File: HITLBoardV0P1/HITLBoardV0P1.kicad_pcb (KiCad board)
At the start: 2 copper layers, 269 parts, among them J2 FTSH-105-01-L-DV, Q1 NPN, Q2 PMOS, Q3 NPN, Q4 PMOS, SW1 SW_Push, SW2 SW_Push, U1 TMDX570LC43HDK_Connectors, U10 DAC7750IPWPR, U11 NC7SZ04P5X, U12 SN74LVC1G08DCKR, U13 NC7SZ04P5X, U14 SN74LVC1G08DCKR, U15 DAC7750IPWPR, U16 NC7SZ04P5X, U17 SN74LVC1G08DCKR, U18 DAC7750IPWPR, U19 NC7SZ04P5X, U2 LAN8650B1-E/LMX, U20 SN74LVC1G08DCKR, U21 DAC7750IPWPR, U22 TLV4387PWR, U23 ADS131M04QPWRQ1, U24 MCP23008-E/SO, U3 LP38852MRX-ADJ/NOPB, U4 LAN8650B1-E/LMX, U5 LP38852MRX-ADJ/NOPB, U6 LAN8650B1-E/LMX, U7 LP38852MRX-ADJ/NOPB, U8 LAN8650B1-E/LMX, U9 LP38852MRX-ADJ/NOPB

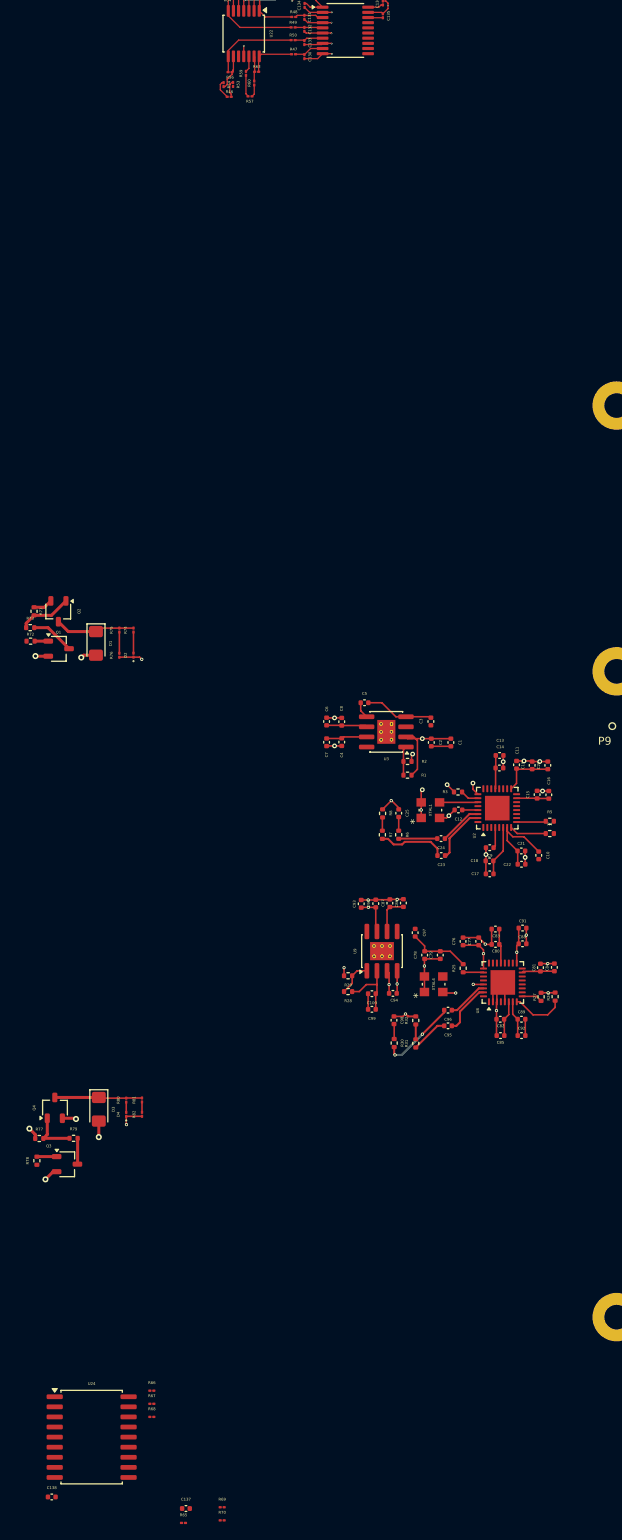
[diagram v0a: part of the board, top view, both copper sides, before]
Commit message: FIX spi 3 on tmdx for current loop ADC, add gpio pin for data ready
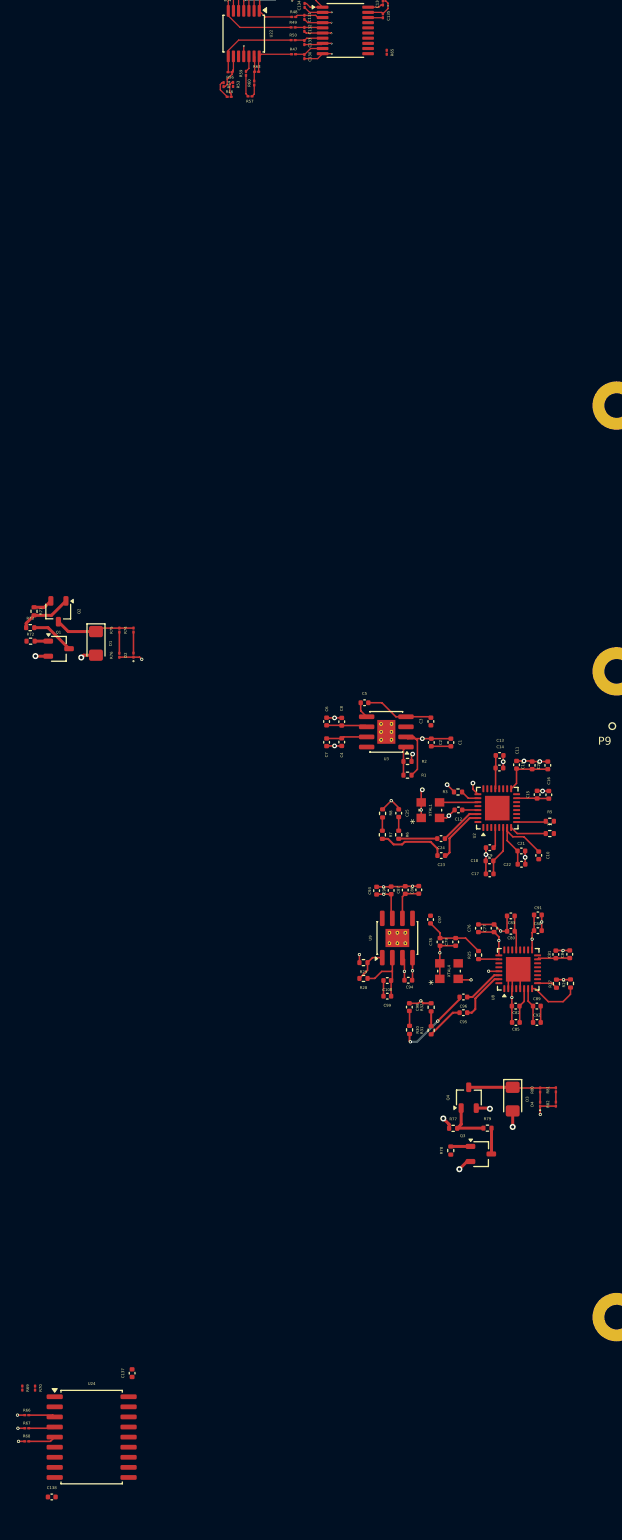
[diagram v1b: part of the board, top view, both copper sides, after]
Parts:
- moved R65 186.9 mm to (95.6, 45.4), turned to -90 degrees
- moved D3 52.1 mm to (111.5, 177.2)
- moved Q4 52.1 mm to (105.9, 177.0)
- moved D4 52.1 mm to (114.9, 177.9)
- moved Q3 52.1 mm to (107.5, 184.1)
- moved R77 52.1 mm to (104.0, 180.9)
- moved R78 52.1 mm to (103.7, 183.7)
- moved R79 52.1 mm to (108.3, 180.9)
- moved R80 52.1 mm to (114.9, 176.1)
- moved R81 52.1 mm to (116.9, 176.0)
- moved R82 52.1 mm to (116.9, 177.8)
- moved R69 29.3 mm to (49.7, 213.6), turned to -90 degrees
- moved R70 28.8 mm to (51.3, 213.6), turned to -90 degrees
- moved C137 18.3 mm to (63.6, 211.7), turned to 90 degrees
- moved R66 16.0 mm to (50.3, 217.0)
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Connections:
- net /TMDX_Breakout/SPI5_CS1_NR renamed /TMDX_Breakout/SPI5_CS1_N
- C137 pad 1: unconnected-(C137-Pad1) -> +3V3
- R68 pad 2: /I2C_GPIO_EXPANDER/<NO NET> -> /I2C_GPIO_EXPANDER/A0
- U1 pad P9-16: /TMDX_Breakout/SPI5_SCLK -> /TMDX_SPI5_SCLK
- U1 pad P9-18: /TMDX_Breakout/SPI5_CS0_N -> /TMDX_SPI5_CS0_N
- U1 pad P9-21: /TMDX_Breakout/SPI5_SIMO_0 -> /TMDX_SPI5_SIMO
- U1 pad P9-22: /TMDX_Breakout/SPI5_SOMI_0 -> /TMDX_SPI5_SOMI
- U24 pad 5: unconnected-(U24-A0-Pad5) -> /I2C_GPIO_EXPANDER/A0
- U8 pad 10: /TMDX_SPI1_SOMI -> /TMDX_SPI5_SOMI
- U8 pad 11: /TMDX_SPI1_CS1 -> /TMDX_SPI5_CS0_N
- U8 pad 12: /TMDX_SPI1_SCLK -> /TMDX_SPI5_SCLK
- U8 pad 13: /TMDX_SPI1_SIMO -> /TMDX_SPI5_SIMO
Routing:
- net /I2C_GPIO_EXPANDER/A1: track 0.00 -> 3.58 mm
- net /I2C_GPIO_EXPANDER/A0: track 0.00 -> 3.49 mm
- net /I2C_GPIO_EXPANDER/A2: track 0.00 -> 3.36 mm
- net GND: track 290.1 -> 292.7 mm, vias 92 -> 95

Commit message: basic organization into layout
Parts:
- removed R84: 10K, Resistor_SMD:R_01005_0402Metric
- removed SW2: SW_Push, Button_Switch_SMD:SW_Push_1P1T_NO_E-Switch_TL3301NxxxxxG
- moved R69 298.8 mm to (330.4, 111.0)
- moved C138 297.8 mm to (333.0, 124.5)
- moved R66 297.8 mm to (329.8, 114.2)
- moved R67 297.8 mm to (329.8, 115.8)
- moved R68 297.8 mm to (329.8, 117.5)
- moved U24 297.8 mm to (338.0, 116.9)
- moved R70 295.9 mm to (328.8, 111.0)
- moved R62 230.0 mm to (253.1, 183.3), turned to 180 degrees
- moved R58 229.9 mm to (252.2, 184.4), turned to 180 degrees
- moved R64 228.6 mm to (253.1, 182.2), turned to 0 degrees
- moved R45 227.2 mm to (249.8, 185.0), turned to 0 degrees
- moved R61 226.8 mm to (251.7, 182.5), turned to 90 degrees
- moved R51 226.3 mm to (250.5, 183.5), turned to 90 degrees
- moved R52 224.4 mm to (249.3, 183.5), turned to 90 degrees
- moved R55 222.5 mm to (249.3, 182.0), turned to 180 degrees
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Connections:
- net /ADC_DRDY renamed /CurrentInstrument/DATA_READY
- C136 pad 1: Net-(U23-DVDD) -> +3V3
- C69 pad 1: +5V -> /ethernet3/U3_BIAS
- R65 pad 1: /ADC_CS_N -> /TMDX_SPI3_CS1_N
- U1 pad P11-73: unconnected-(U1C-SPI3_SIMO-PadP11-73) -> /TMDX_SPI3_SIMO
- U1 pad P11-74: unconnected-(U1C-SPI3_SOMI-PadP11-74) -> /TMDX_SPI3_SOMI
- U1 pad P11-75: unconnected-(U1C-SPI3_CS1_NHET125-PadP11-75) -> /TMDX_SPI3_CS1_N
- U1 pad P11-78: unconnected-(U1C-SPI3_CLK-PadP11-78) -> /TMDX_SPI3_SCLK
- U23 pad 12: /ADC_CS_N -> /TMDX_SPI3_CS1_N
- U23 pad 14: /CurrentInstrument/SCLK -> /TMDX_SPI3_SCLK
- U23 pad 15: /CurrentInstrument/SDO -> /TMDX_SPI3_SOMI
- U23 pad 16: /CurrentInstrument/SDI -> /TMDX_SPI3_SIMO
- U23 pad 20: Net-(U23-DVDD) -> +3V3
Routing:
- net /RPI_I2C_SDA: track 0.00 -> 5.30 mm
- net /RPI_I2C_SCL: track 0.00 -> 3.20 mm
- net +3.3VP: track 30.7 -> 33.5 mm, vias 6 -> 9
- net +3V3: track 151.1 -> 153.8 mm, vias 26 -> 27
- net /TMDX_SPI3_CS1_N: track 0.00 -> 2.44 mm
- net Net-(U23-DVDD): track 1.98 -> 0.00 mm
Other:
- board outline added: 275.4 x 125.2 mm
- board text removed: "RPI BOOTSEL"

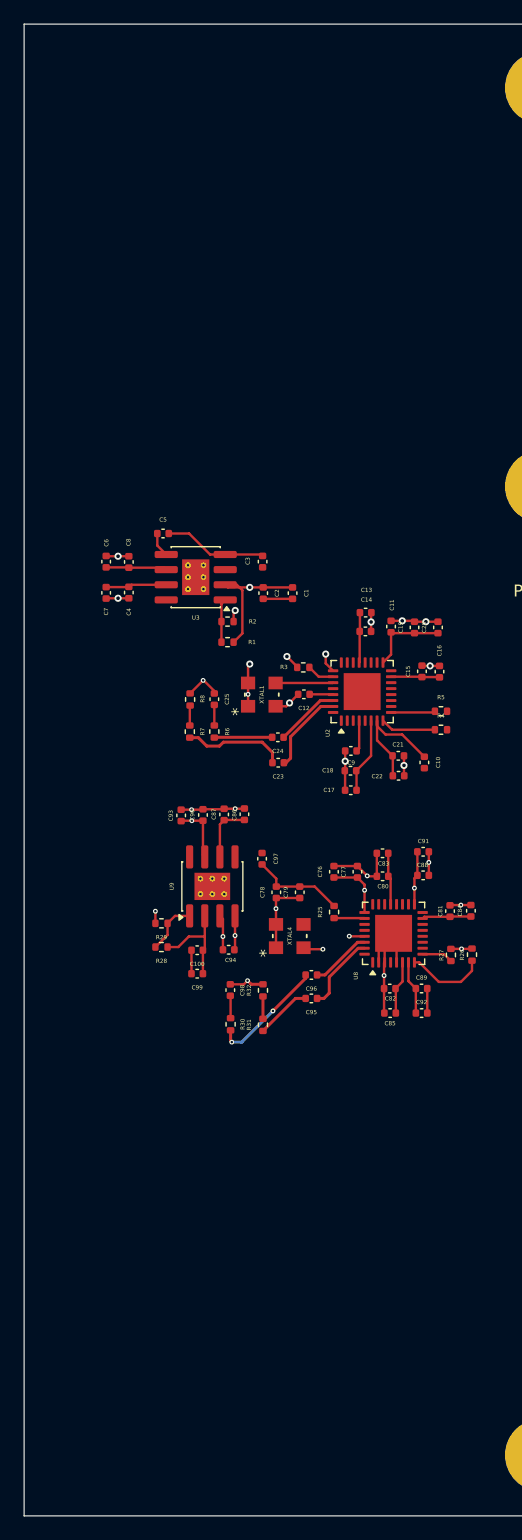
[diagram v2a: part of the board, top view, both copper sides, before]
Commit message: fix ethernet channel that was fubar, beginning layout
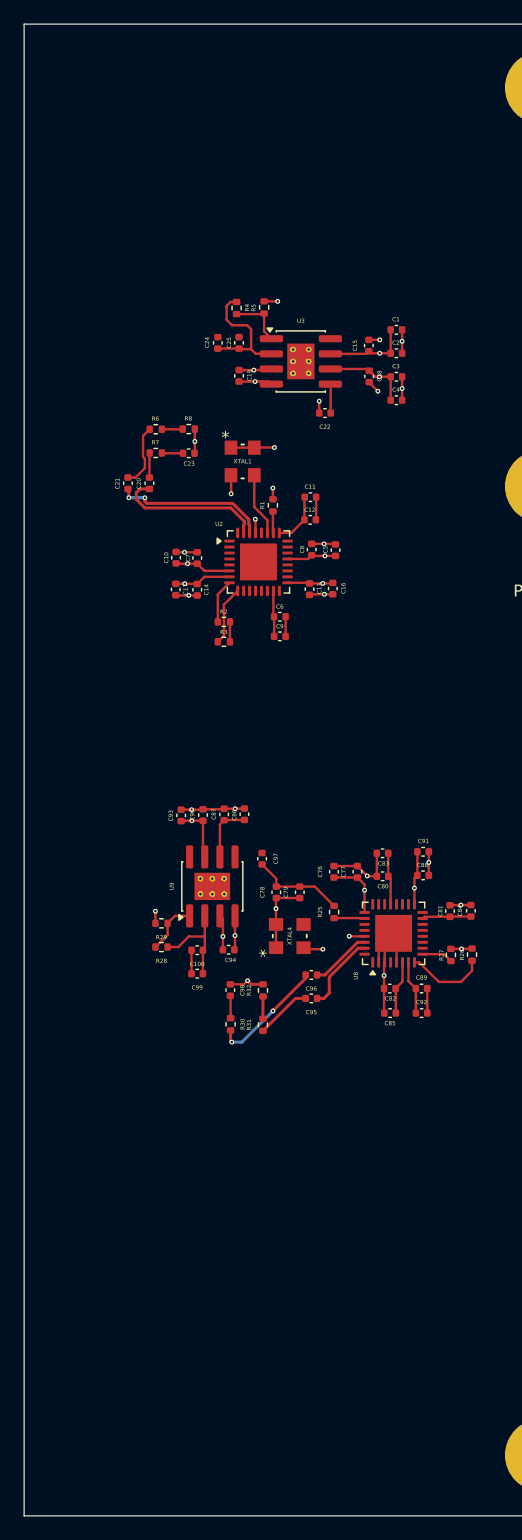
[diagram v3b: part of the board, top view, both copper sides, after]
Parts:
- moved R4 39.3 mm to (99.0, 108.4), turned to -90 degrees
- moved R5 37.0 mm to (101.3, 108.3), turned to 90 degrees
- moved C24 33.5 mm to (97.4, 111.3), turned to 90 degrees
- moved C18 33.1 mm to (110.1, 114.1), turned to -90 degrees
- moved C21 32.2 mm to (89.9, 123.1), turned to 90 degrees
- moved C22 31.1 mm to (106.4, 117.2), turned to 180 degrees
- moved C25 30.0 mm to (99.2, 111.3), turned to 90 degrees
- moved C15 27.7 mm to (110.1, 111.5)
- moved C4 27.7 mm to (112.4, 116.1), turned to 0 degrees
- moved C20 27.1 mm to (91.7, 123.1)
- moved C23 27.0 mm to (95.0, 120.6)
- moved C10 27.0 mm to (93.9, 129.3), turned to 90 degrees
- moved R6 25.8 mm to (92.2, 118.6), turned to 0 degrees
- moved C19 25.7 mm to (99.2, 114.1), turned to -90 degrees
- moved C1 23.8 mm to (112.4, 110.2), turned to 0 degrees
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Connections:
- C10 pad 1: +3V3 -> /Ethernet/1V8_U2
- C5 pad 1: +3V3 -> /Ethernet/1V8_U2
- C6 pad 1: +3V3 -> /Ethernet/1V8_U2
- C69 pad 1: /ethernet3/U3_BIAS -> +5V
- C7 pad 1: +3V3 -> /Ethernet/1V8_U2
- C8 pad 1: +3V3 -> /Ethernet/1V8_U2
- C9 pad 1: +3V3 -> /Ethernet/1V8_U2
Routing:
- net GND: track 292.7 -> 274.8 mm, vias 95 -> 99
- net /Ethernet/1V8_U2: track 36.8 -> 23.6 mm, vias 1 -> 2
- net /Ethernet/TRX_DP: track 0.00 -> 12.9 mm, vias 0 -> 2
- net /Ethernet/TRX_DN: track 0.00 -> 12.6 mm
- net Net-(C23-Pad2): track 10.3 -> 3.54 mm
- net +3V3: track 153.8 -> 148.1 mm, vias 27 -> 28
- net /Ethernet/ETH_10T1S_TRX_DP: track 0.00 -> 5.30 mm
- net /LAN1_IRQ_N: track 0.00 -> 4.96 mm
- net /RESET_N: track 19.6 -> 23.2 mm
- net +5V: track 9.30 -> 12.1 mm, vias 3 -> 4
- net /Ethernet/U3_ADJ: track 7.39 -> 4.70 mm
- net /Ethernet/ETH_10T1S_TRX_DN: track 0.00 -> 2.07 mm
- net (no net): track 1.73 -> 0.00 mm

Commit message: layout in progress
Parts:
- moved R18 56.3 mm to (286.3, 127.5), turned to 90 degrees
- moved C138 18.1 mm to (343.3, 109.7)
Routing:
- net /RPI_SPI1_MOSI: track 0.00 -> 135.5 mm, vias 0 -> 7
- net /RPI_SPI1_MISO: track 0.00 -> 124.1 mm, vias 0 -> 5
- net /RPI_SPI0_SCK: track 0.00 -> 52.2 mm, vias 0 -> 2
- net /RPI_SPI0_MOSI: track 0.00 -> 48.6 mm, vias 0 -> 2
- net /SPI0_CS0: track 0.00 -> 35.9 mm
- net GND: track 274.8 -> 305.3 mm, vias 99 -> 110
- net /GPIO_XPNDR_IRQ: track 0.00 -> 30.2 mm
- net /SPI0_CS1: track 0.00 -> 23.7 mm, vias 0 -> 2
- net /IRQ_N_1: track 3.18 -> 22.3 mm, vias 0 -> 2
- net /RPI_SPI0_MISO: track 0.00 -> 17.1 mm, vias 0 -> 2
- net /RESET_N: track 23.2 -> 38.0 mm
- net /RPI_I2C_SCL: track 3.20 -> 16.2 mm
- net /RPI_I2C_SDA: track 5.30 -> 15.2 mm
- net +3.3VP: track 33.5 -> 38.3 mm, vias 9 -> 10
- net /LED2: track 0.00 -> 4.03 mm
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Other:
- copper layers 2 -> 8
